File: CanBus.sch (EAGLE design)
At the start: 59 parts, among them IC1 MCP2515-I/SO, IC2 MEGA8-AI, IC3 MCP2515-I/SO, Q1 16MHz, Q2 16MHz, Q3 16MHz, U1 MCP2562-E/SN, U2 MCP2562-E/SN, X1 MAC64L

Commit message: Layouts angepasst
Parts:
- added J2, J3: (no value), mebp_8-8g:555141-1
- added JP1, JP3: (no value), jumper:JP1E
- added R10, R9: 4k7, rcl:R-EU_R1206
- R1, R4: value 4k7 -> 120R
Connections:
- new net CANH_1: J1.7, J2.2, R1.1
- new net CANH_3: J3.7, R3.1
- new net CANL_1: J1.8, J2.1, JP1.2
- new net CANL_3: J3.8, JP3.2
- new net N$12: JP3.1, R3.2
- new net N$8: JP1.1, R1.2
- net +24V: now also J2.4, J2.5, J3.4, J3.5
- net +3,3V: now also R10.2, R9.2; no longer R1.2, R4.2
- net CANH: now also R4.1; no longer R2.1
- net CANH_2: now also J2.7, J3.2, R2.1; no longer J1.7, R3.1
- net CANL: now also R4.2; no longer R2.2
- net CANL_2: now also J2.8, J3.1; no longer J1.8
- net GND: now also J2.3, J2.6, J2.S1, J2.S2, J3.3, J3.6, J3.S1, J3.S2
- net N$2: now also R9.1; no longer R1.1
- net N$3: now also R2.2; no longer R3.2
- net N$5: now also R10.1; no longer R4.1
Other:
- moved on the sheet: J1, R1, R2, R3

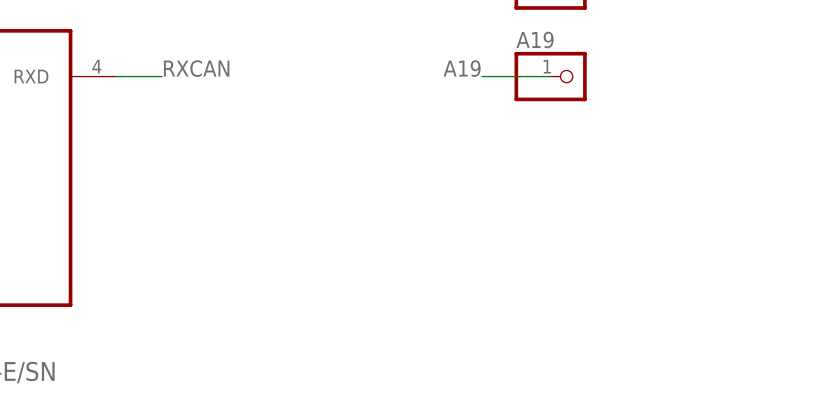
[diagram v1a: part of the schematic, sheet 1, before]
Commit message: Schaltpläne aufgehübscht zur Veröffentlichung
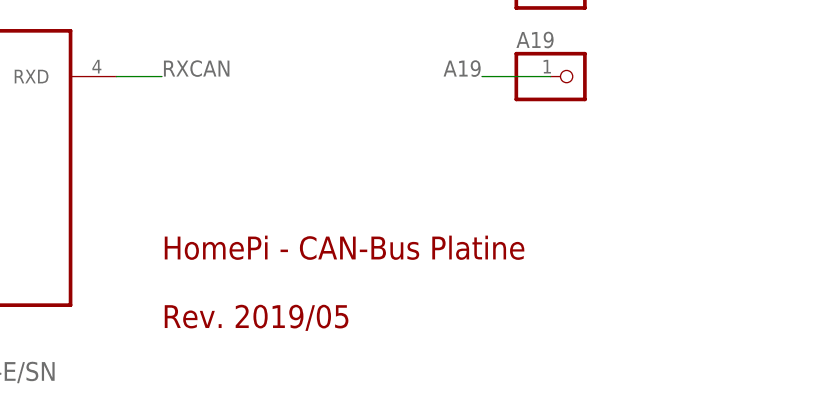
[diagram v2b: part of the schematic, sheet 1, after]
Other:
- note added: "HomePi - CAN-Bus Platine Rev. 2019/05"
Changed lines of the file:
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@@
 <sheet>
 <plain>
+<text x="160.02" y="15.24" size="2.54" layer="94" align="top-left">HomePi - CAN-Bus Platine
+Rev. 2019/05</text>
 </plain>
 <instances>
@@
 <sheet>
 <plain>
+<text x="160.02" y="15.24" size="2.54" layer="94" align="top-left">HomePi - CAN-Bus Platine
+Rev. 2019/05</text>
 </plain>
 <instances>
@@
 </schematic>
 </drawing>
+<compatibility>
+<note version="6.3" minversion="6.2.2" severity="warning">
+Since Version 6.2.2 text objects can contain more than one line,
+which will not be processed correctly with this version.
+</note>
+</compatibility>
 </eagle>
